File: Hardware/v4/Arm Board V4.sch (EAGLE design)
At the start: 38 parts, among them IC3 L6206D, P1 STELLARIS-LAUNCHPADSTELLARIS-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, U1 SN74LS241DW, U2 XBEE-1B3

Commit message: added cap
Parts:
- added C1: (no value), SparkFun-Capacitors:CAP_POLE
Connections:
- net +12V: now also C1.+
- net GND: now also C1.-
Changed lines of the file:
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@@
 <part name="R15" library="SparkFun-Resistors" deviceset="RESISTOR" device="1206" value="100"/>
 <part name="U$6" library="MRDT-2015-PowerBoard" deviceset="H_WR-TBL_32*1*0002" device="VERT"/>
+<part name="C1" library="SparkFun-Capacitors" deviceset="CAP_POL" device="E"/>
+<part name="GND3" library="SparkFun-Aesthetics" deviceset="GND" device=""/>
 </parts>
 <sheets>
@@
 <instance part="D1" gate="G$1" x="22.86" y="10.16"/>
 <instance part="U$6" gate="G$1" x="132.08" y="10.16"/>
+<instance part="C1" gate="G$1" x="127" y="-40.64" rot="R90"/>
+<instance part="GND3" gate="1" x="134.62" y="-40.64" rot="R90"/>
 </instances>
 <busses>
@@
 <wire x1="172.72" y1="7.62" x2="167.64" y2="7.62" width="0.1524" layer="91"/>
 </segment>
+<segment>
+<pinref part="C1" gate="G$1" pin="-"/>
+<pinref part="GND3" gate="1" pin="GND"/>
+</segment>
 </net>
 <net name="+12V" class="0">
@@
 <wire x1="172.72" y1="22.86" x2="167.64" y2="22.86" width="0.1524" layer="91"/>
 </segment>
+<segment>
+<pinref part="C1" gate="G$1" pin="+"/>
+<wire x1="124.46" y1="-40.64" x2="119.38" y2="-40.64" width="0.1524" layer="91"/>
+<label x="124.46" y="-38.1" size="1.778" layer="95" rot="R180"/>
+</segment>
 </net>

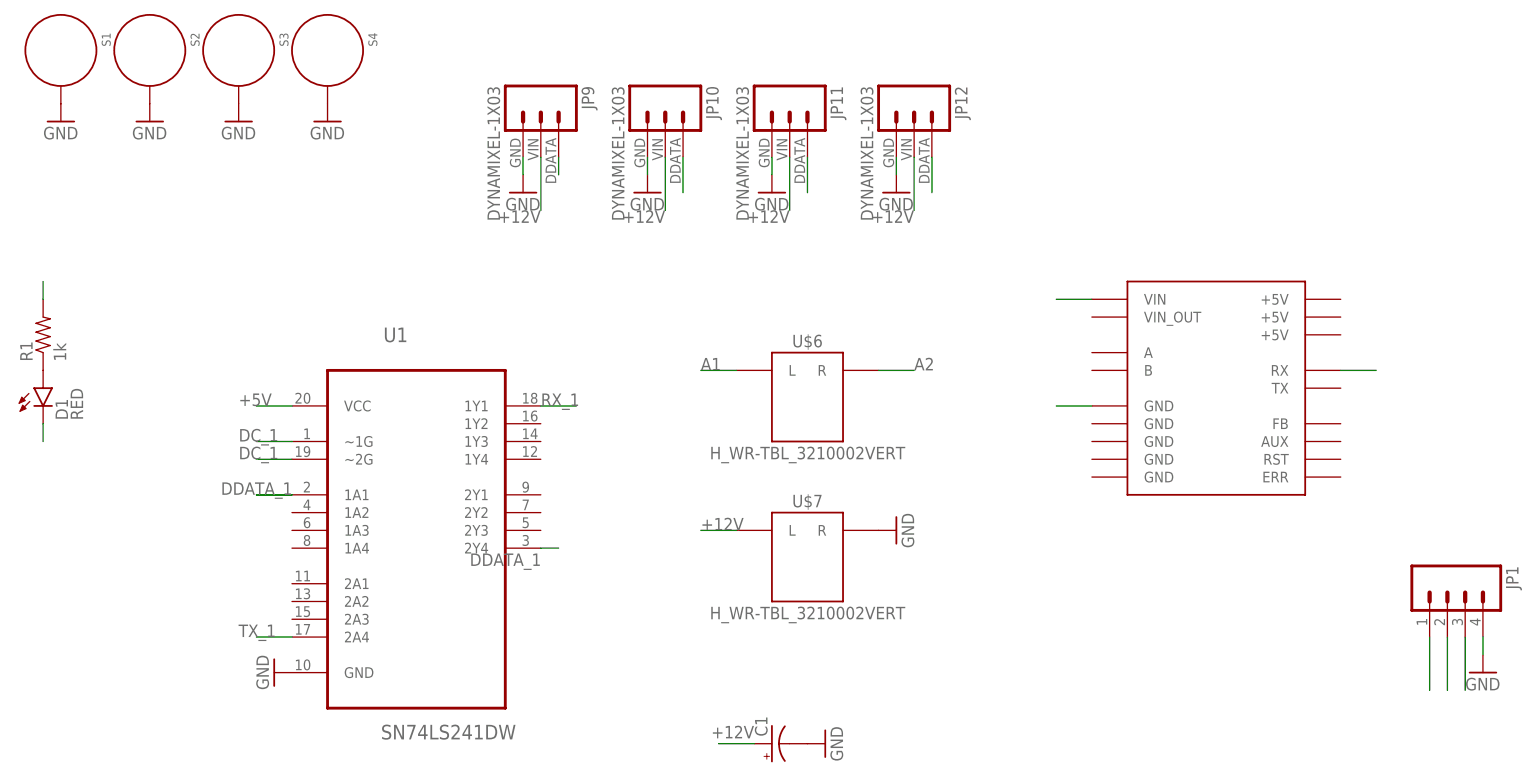
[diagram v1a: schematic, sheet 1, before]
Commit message: added cap, rerouted
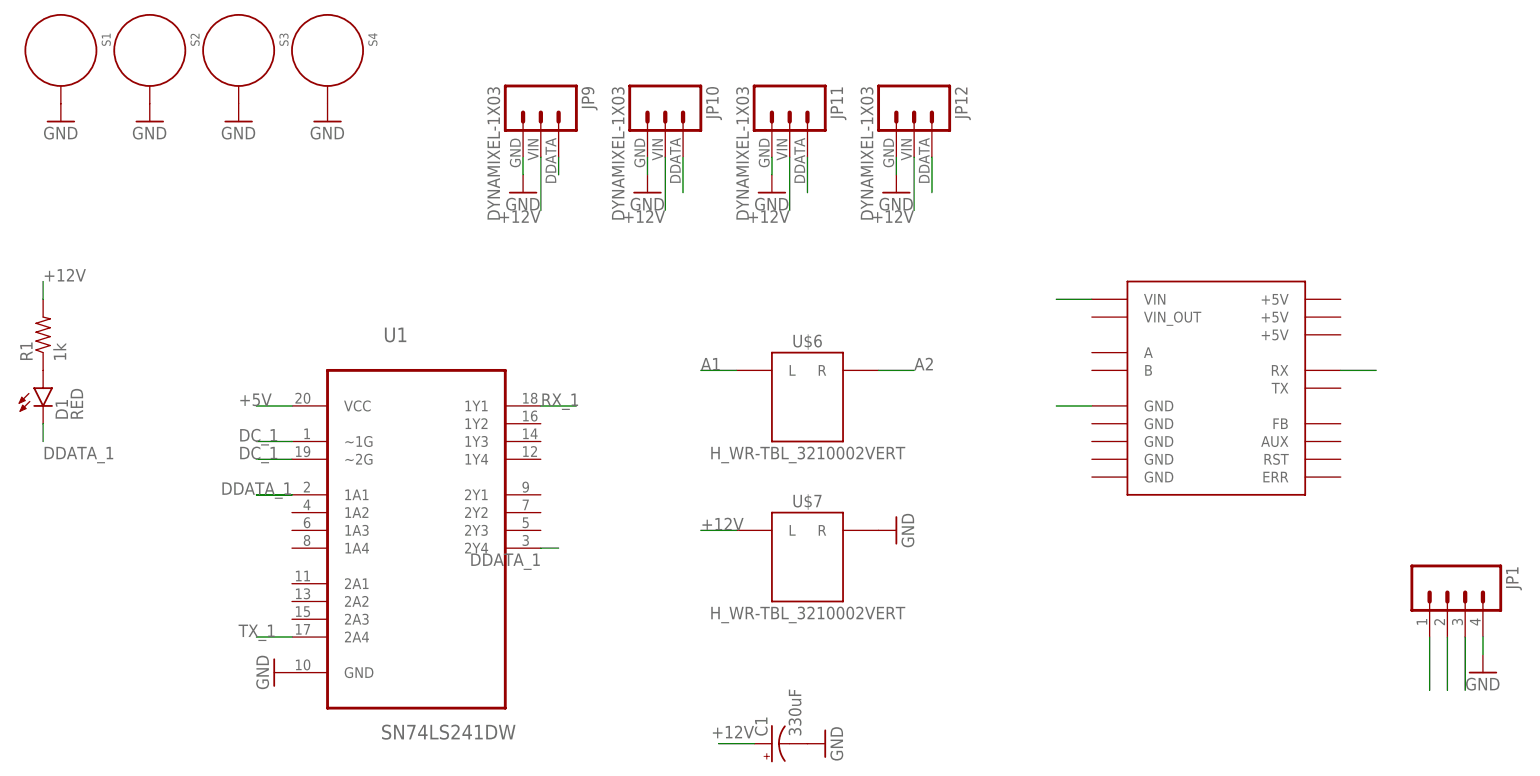
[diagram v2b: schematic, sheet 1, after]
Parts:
- C1: value (none) -> 330uF
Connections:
- net +12V: now also R1.2
- net +5V: no longer R1.2
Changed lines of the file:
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@@
 <part name="R15" library="SparkFun-Resistors" deviceset="RESISTOR" device="1206" value="100"/>
 <part name="U$6" library="MRDT-2015-PowerBoard" deviceset="H_WR-TBL_32*1*0002" device="VERT"/>
-<part name="C1" library="SparkFun-Capacitors" deviceset="CAP_POL" device="E"/>
+<part name="C1" library="SparkFun-Capacitors" deviceset="CAP_POL" device="E" value="330uF"/>
 <part name="GND3" library="SparkFun-Aesthetics" deviceset="GND" device=""/>
 </parts>
@@
 <label x="124.46" y="-38.1" size="1.778" layer="95" rot="R180"/>
 </segment>
+<segment>
+<pinref part="R1" gate="G$1" pin="2"/>
+<wire x1="22.86" y1="22.86" x2="22.86" y2="25.4" width="0.1524" layer="91"/>
+<label x="22.86" y="25.4" size="1.778" layer="95"/>
+</segment>
 </net>
 <net name="+5V" class="0">
@@
 <wire x1="226.06" y1="-25.4" x2="226.06" y2="-33.02" width="0.1524" layer="91"/>
 <pinref part="JP1" gate="G$1" pin="3"/>
-</segment>
-<segment>
-<pinref part="R1" gate="G$1" pin="2"/>
-<wire x1="22.86" y1="22.86" x2="22.86" y2="25.4" width="0.1524" layer="91"/>
 </segment>
 </net>
@@
 <wire x1="22.86" y1="5.08" x2="22.86" y2="2.54" width="0.1524" layer="91"/>
 <pinref part="D1" gate="G$1" pin="C"/>
-</segment>
-</net>
+<label x="22.86" y="0" size="1.778" layer="95"/>
+</segment>
+</net>

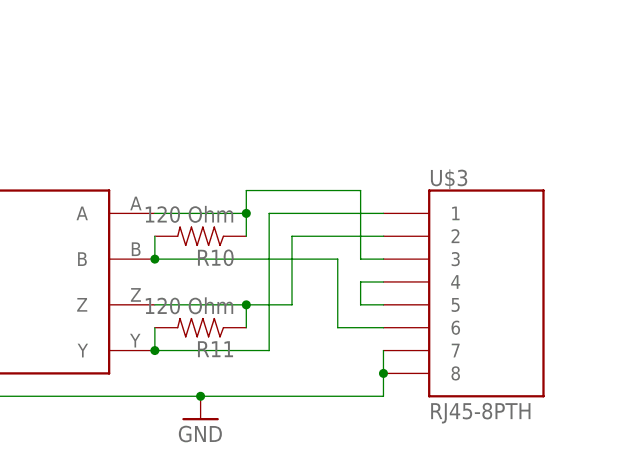
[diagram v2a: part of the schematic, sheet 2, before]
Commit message: cleaned up brd, updated bom
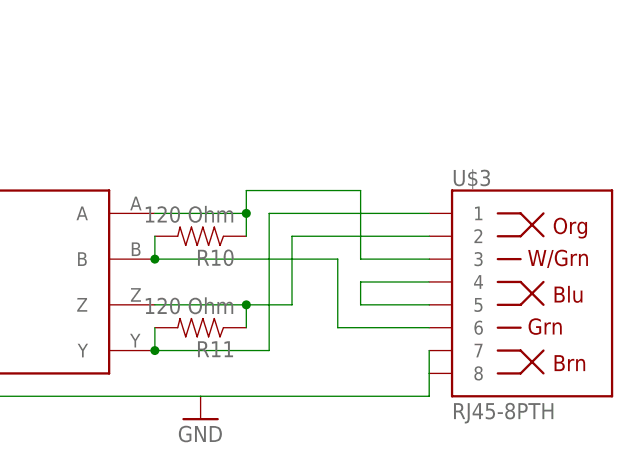
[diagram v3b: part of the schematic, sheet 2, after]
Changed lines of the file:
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@@
 <layer number="223" name="223bmp" color="24" fill="1" visible="no" active="no"/>
 <layer number="224" name="224bmp" color="25" fill="1" visible="no" active="no"/>
+<layer number="225" name="225bmp" color="7" fill="1" visible="yes" active="yes"/>
+<layer number="226" name="226bmp" color="7" fill="1" visible="yes" active="yes"/>
+<layer number="227" name="227bmp" color="7" fill="1" visible="yes" active="yes"/>
+<layer number="228" name="228bmp" color="7" fill="1" visible="yes" active="yes"/>
+<layer number="229" name="229bmp" color="7" fill="1" visible="yes" active="yes"/>
+<layer number="230" name="230bmp" color="7" fill="1" visible="yes" active="yes"/>
 <layer number="231" name="Eagle3D_PG1" color="7" fill="1" visible="no" active="no"/>
 <layer number="232" name="Eagle3D_PG2" color="7" fill="1" visible="no" active="no"/>
@@
 <layer number="251" name="SMDround" color="12" fill="11" visible="no" active="no"/>
 <layer number="254" name="cooling" color="7" fill="1" visible="no" active="yes"/>
+<layer number="255" name="routoute" color="7" fill="1" visible="yes" active="yes"/>
 </layers>
 <schematic xreflabel="%F%N/%S.%C%R" xrefpart="/%S.%C%R">
@@
 <part name="C1" library="SparkFun-Capacitors" deviceset="CAP_POL" device="E" value="330uF"/>
 <part name="GND3" library="SparkFun-Aesthetics" deviceset="GND" device=""/>
+<part name="GND10" library="SparkFun-Aesthetics" deviceset="GND" device=""/>
 </parts>
 <sheets>
@@
 <instance part="C1" gate="G$1" x="127" y="-40.64" rot="R90"/>
 <instance part="GND3" gate="1" x="134.62" y="-40.64" rot="R90"/>
+<instance part="GND10" gate="1" x="170.18" y="7.62" rot="R270"/>
 </instances>
 <busses>
@@
 <segment>
 <pinref part="U$1" gate="G$1" pin="GND@1"/>
-<wire x1="172.72" y1="7.62" x2="167.64" y2="7.62" width="0.1524" layer="91"/>
+<pinref part="GND10" gate="1" pin="GND"/>
 </segment>
 <segment>
@@
 <pinref part="U$1" gate="G$1" pin="VIN"/>
 <wire x1="172.72" y1="22.86" x2="167.64" y2="22.86" width="0.1524" layer="91"/>
+<label x="167.64" y="22.86" size="1.778" layer="95"/>
 </segment>
 <segment>
@@
 <pinref part="U$1" gate="G$1" pin="RX"/>
 <wire x1="208.28" y1="12.7" x2="213.36" y2="12.7" width="0.1524" layer="91"/>
+<label x="208.28" y="12.7" size="1.778" layer="95"/>
 </segment>
 </net>
@@
 </plain>
 <instances>
-<instance part="U$3" gate="G$1" x="144.78" y="12.7"/>
+<instance part="U$3" gate="JP1" x="144.78" y="15.24"/>
 <instance part="R10" gate="G$1" x="111.76" y="20.32" rot="R180"/>
 <instance part="GND7" gate="1" x="111.76" y="0"/>
@@
 <wire x1="71.12" y1="2.54" x2="71.12" y2="7.62" width="0.1524" layer="91"/>
 <wire x1="71.12" y1="7.62" x2="76.2" y2="7.62" width="0.1524" layer="91"/>
-<junction x="111.76" y="2.54"/>
 <pinref part="C12" gate="G$1" pin="2"/>
 <wire x1="66.04" y1="15.24" x2="66.04" y2="2.54" width="0.1524" layer="91"/>
 <wire x1="66.04" y1="2.54" x2="71.12" y2="2.54" width="0.1524" layer="91"/>
 <junction x="71.12" y="2.54"/>
-<pinref part="U$3" gate="G$1" pin="8"/>
-<pinref part="U$3" gate="G$1" pin="7"/>
-<wire x1="132.08" y1="7.62" x2="132.08" y2="5.08" width="0.1524" layer="91"/>
-<junction x="132.08" y="5.08"/>
-<wire x1="132.08" y1="5.08" x2="132.08" y2="2.54" width="0.1524" layer="91"/>
-<wire x1="111.76" y1="2.54" x2="132.08" y2="2.54" width="0.1524" layer="91"/>
 <pinref part="U$4" gate="G$1" pin="GND"/>
+<pinref part="U$3" gate="JP1" pin="8"/>
+<pinref part="U$3" gate="JP1" pin="7"/>
+<wire x1="137.16" y1="7.62" x2="137.16" y2="5.08" width="0.1524" layer="91"/>
+<wire x1="137.16" y1="5.08" x2="137.16" y2="2.54" width="0.1524" layer="91"/>
+<wire x1="137.16" y1="2.54" x2="111.76" y2="2.54" width="0.1524" layer="91"/>
 </segment>
 <segment>
@@
 <wire x1="106.68" y1="7.62" x2="119.38" y2="7.62" width="0.1524" layer="91"/>
 <wire x1="119.38" y1="7.62" x2="119.38" y2="22.86" width="0.1524" layer="91"/>
-<pinref part="U$3" gate="G$1" pin="1"/>
-<wire x1="119.38" y1="22.86" x2="132.08" y2="22.86" width="0.1524" layer="91"/>
+<pinref part="U$3" gate="JP1" pin="1"/>
+<wire x1="119.38" y1="22.86" x2="137.16" y2="22.86" width="0.1524" layer="91"/>
 <pinref part="R11" gate="G$1" pin="2"/>
 <wire x1="106.68" y1="7.62" x2="106.68" y2="10.16" width="0.1524" layer="91"/>
@@
 <wire x1="116.84" y1="12.7" x2="121.92" y2="12.7" width="0.1524" layer="91"/>
 <wire x1="121.92" y1="12.7" x2="121.92" y2="20.32" width="0.1524" layer="91"/>
-<pinref part="U$3" gate="G$1" pin="2"/>
-<wire x1="121.92" y1="20.32" x2="132.08" y2="20.32" width="0.1524" layer="91"/>
+<pinref part="U$3" gate="JP1" pin="2"/>
+<wire x1="121.92" y1="20.32" x2="137.16" y2="20.32" width="0.1524" layer="91"/>
 <pinref part="R11" gate="G$1" pin="1"/>
 <wire x1="116.84" y1="10.16" x2="116.84" y2="12.7" width="0.1524" layer="91"/>
@@
 <wire x1="106.68" y1="17.78" x2="127" y2="17.78" width="0.1524" layer="91"/>
 <wire x1="127" y1="17.78" x2="127" y2="10.16" width="0.1524" layer="91"/>
-<pinref part="U$3" gate="G$1" pin="6"/>
-<wire x1="127" y1="10.16" x2="132.08" y2="10.16" width="0.1524" layer="91"/>
+<pinref part="U$3" gate="JP1" pin="6"/>
+<wire x1="127" y1="10.16" x2="137.16" y2="10.16" width="0.1524" layer="91"/>
 <pinref part="R10" gate="G$1" pin="2"/>
 <wire x1="106.68" y1="17.78" x2="106.68" y2="20.32" width="0.1524" layer="91"/>
@@
 <wire x1="116.84" y1="25.4" x2="129.54" y2="25.4" width="0.1524" layer="91"/>
 <wire x1="129.54" y1="25.4" x2="129.54" y2="17.78" width="0.1524" layer="91"/>
-<pinref part="U$3" gate="G$1" pin="3"/>
-<wire x1="129.54" y1="17.78" x2="132.08" y2="17.78" width="0.1524" layer="91"/>
+<pinref part="U$3" gate="JP1" pin="3"/>
+<wire x1="129.54" y1="17.78" x2="137.16" y2="17.78" width="0.1524" layer="91"/>
 <pinref part="R10" gate="G$1" pin="1"/>
 <wire x1="116.84" y1="20.32" x2="116.84" y2="22.86" width="0.1524" layer="91"/>
@@
 </segment>
 <segment>
-<pinref part="U$3" gate="G$1" pin="4"/>
-<wire x1="132.08" y1="15.24" x2="129.54" y2="15.24" width="0.1524" layer="91"/>
+<pinref part="U$3" gate="JP1" pin="4"/>
+<wire x1="137.16" y1="15.24" x2="129.54" y2="15.24" width="0.1524" layer="91"/>
 <wire x1="129.54" y1="15.24" x2="129.54" y2="12.7" width="0.1524" layer="91"/>
-<pinref part="U$3" gate="G$1" pin="5"/>
-<wire x1="129.54" y1="12.7" x2="132.08" y2="12.7" width="0.1524" layer="91"/>
-</segment>
-<segment>
+<pinref part="U$3" gate="JP1" pin="5"/>
+<wire x1="129.54" y1="12.7" x2="137.16" y2="12.7" width="0.1524" layer="91"/>
+</segment>
+<segment>

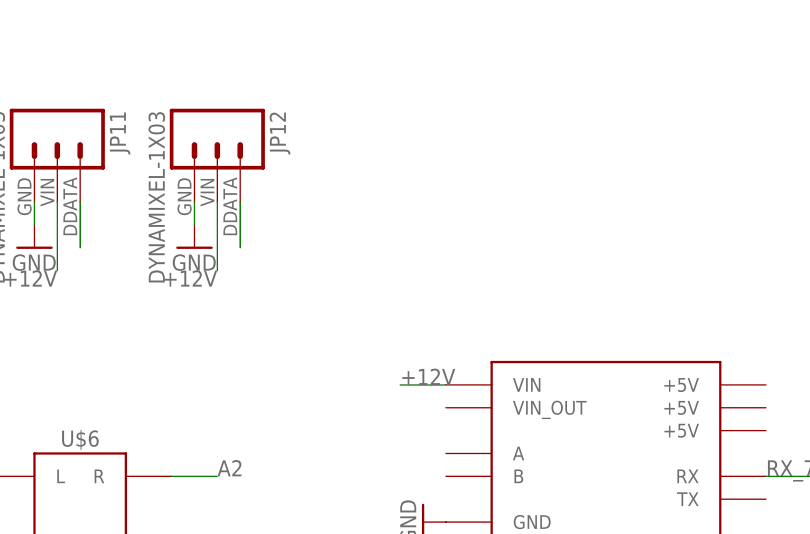
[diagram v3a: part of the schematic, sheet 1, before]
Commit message: Added TVS diodes on Dyna data lines
Also added parts to BOM
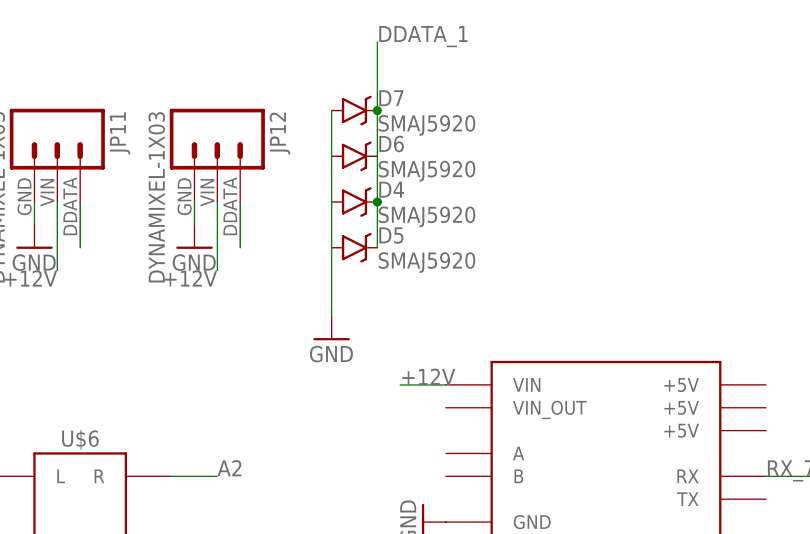
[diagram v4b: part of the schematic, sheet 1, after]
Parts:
- added D4, D5, D6, D7: SMAJ5920, SparkFun-DiscreteSemi:DIODE-SCHOTTKY-MBRA140
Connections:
- net DDATA_1: now also D4.C, D5.C, D6.C, D7.C
- net GND: now also D4.A, D5.A, D6.A, D7.A
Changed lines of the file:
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@@
 <?xml version="1.0" encoding="utf-8"?>
 <!DOCTYPE eagle SYSTEM "eagle.dtd">
-<eagle version="6.5.0">
+<eagle version="7.0.0">
 <drawing>
 <settings>
@@
 <part name="GND3" library="SparkFun-Aesthetics" deviceset="GND" device=""/>
 <part name="GND10" library="SparkFun-Aesthetics" deviceset="GND" device=""/>
+<part name="D4" library="SparkFun-DiscreteSemi" deviceset="DIODE-SCHOTTKY" device="-MBRA140" value="SMAJ5920"/>
+<part name="D5" library="SparkFun-DiscreteSemi" deviceset="DIODE-SCHOTTKY" device="-MBRA140" value="SMAJ5920"/>
+<part name="D6" library="SparkFun-DiscreteSemi" deviceset="DIODE-SCHOTTKY" device="-MBRA140" value="SMAJ5920"/>
+<part name="D7" library="SparkFun-DiscreteSemi" deviceset="DIODE-SCHOTTKY" device="-MBRA140" value="SMAJ5920"/>
+<part name="GND15" library="SparkFun-Aesthetics" deviceset="GND" device=""/>
 </parts>
 <sheets>
@@
 <instance part="GND3" gate="1" x="134.62" y="-40.64" rot="R90"/>
 <instance part="GND10" gate="1" x="170.18" y="7.62" rot="R270"/>
+<instance part="D4" gate="G$1" x="162.56" y="43.18"/>
+<instance part="D5" gate="G$1" x="162.56" y="38.1"/>
+<instance part="D6" gate="G$1" x="162.56" y="48.26"/>
+<instance part="D7" gate="G$1" x="162.56" y="53.34"/>
+<instance part="GND15" gate="1" x="160.02" y="27.94"/>
 </instances>
 <busses>
@@
 <pinref part="GND3" gate="1" pin="GND"/>
 </segment>
+<segment>
+<pinref part="D7" gate="G$1" pin="A"/>
+<pinref part="D6" gate="G$1" pin="A"/>
+<wire x1="160.02" y1="53.34" x2="160.02" y2="48.26" width="0.1524" layer="91"/>
+<pinref part="D4" gate="G$1" pin="A"/>
+<wire x1="160.02" y1="48.26" x2="160.02" y2="43.18" width="0.1524" layer="91"/>
+<pinref part="D5" gate="G$1" pin="A"/>
+<wire x1="160.02" y1="43.18" x2="160.02" y2="38.1" width="0.1524" layer="91"/>
+<wire x1="160.02" y1="38.1" x2="160.02" y2="30.48" width="0.1524" layer="91"/>
+<pinref part="GND15" gate="1" pin="GND"/>
+</segment>
 </net>
 <net name="+12V" class="0">
@@
 <label x="22.86" y="0" size="1.778" layer="95"/>
 </segment>
+<segment>
+<pinref part="D5" gate="G$1" pin="C"/>
+<wire x1="165.1" y1="60.96" x2="165.1" y2="53.34" width="0.1524" layer="91"/>
+<pinref part="D6" gate="G$1" pin="C"/>
+<wire x1="165.1" y1="53.34" x2="165.1" y2="48.26" width="0.1524" layer="91"/>
+<wire x1="165.1" y1="38.1" x2="165.1" y2="43.18" width="0.1524" layer="91"/>
+<pinref part="D7" gate="G$1" pin="C"/>
+<junction x="165.1" y="53.34"/>
+<pinref part="D4" gate="G$1" pin="C"/>
+<wire x1="165.1" y1="43.18" x2="165.1" y2="48.26" width="0.1524" layer="91"/>
+<junction x="165.1" y="43.18"/>
+<label x="165.1" y="60.96" size="1.778" layer="95"/>
+</segment>
 </net>

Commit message: added some trace names
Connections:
- net N$1 renamed TX-
- net N$2 renamed RX-
- net N$3 renamed RX+
- net N$5 renamed TX+
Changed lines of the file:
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@@
 <?xml version="1.0" encoding="utf-8"?>
 <!DOCTYPE eagle SYSTEM "eagle.dtd">
-<eagle version="7.0.0">
+<eagle version="6.5.0">
 <drawing>
 <settings>
@@
 </segment>
 </net>
-<net name="N$5" class="0">
+<net name="TX+" class="0">
 <segment>
 <wire x1="106.68" y1="7.62" x2="119.38" y2="7.62" width="0.1524" layer="91"/>
@@
 </segment>
 </net>
-<net name="N$1" class="0">
+<net name="TX-" class="0">
 <segment>
 <wire x1="106.68" y1="12.7" x2="116.84" y2="12.7" width="0.1524" layer="91"/>
@@
 </segment>
 </net>
-<net name="N$2" class="0">
+<net name="RX-" class="0">
 <segment>
 <wire x1="106.68" y1="17.78" x2="127" y2="17.78" width="0.1524" layer="91"/>
@@
 </segment>
 </net>
-<net name="N$3" class="0">
+<net name="RX+" class="0">
 <segment>
 <wire x1="106.68" y1="22.86" x2="116.84" y2="22.86" width="0.1524" layer="91"/>
